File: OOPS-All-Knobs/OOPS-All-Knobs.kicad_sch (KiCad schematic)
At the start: 179 parts, among them J1 USB_C_Receptacle_USB2.0, J2 Conn_01x03_Female, SW1 SW_SPST, SW2 SW_SPST, U1 NCP1117-3.3_SOT223, U2 W25Q128JVS, U3 RP2040TR7, U4 SRV05-4, Y1 12MHz

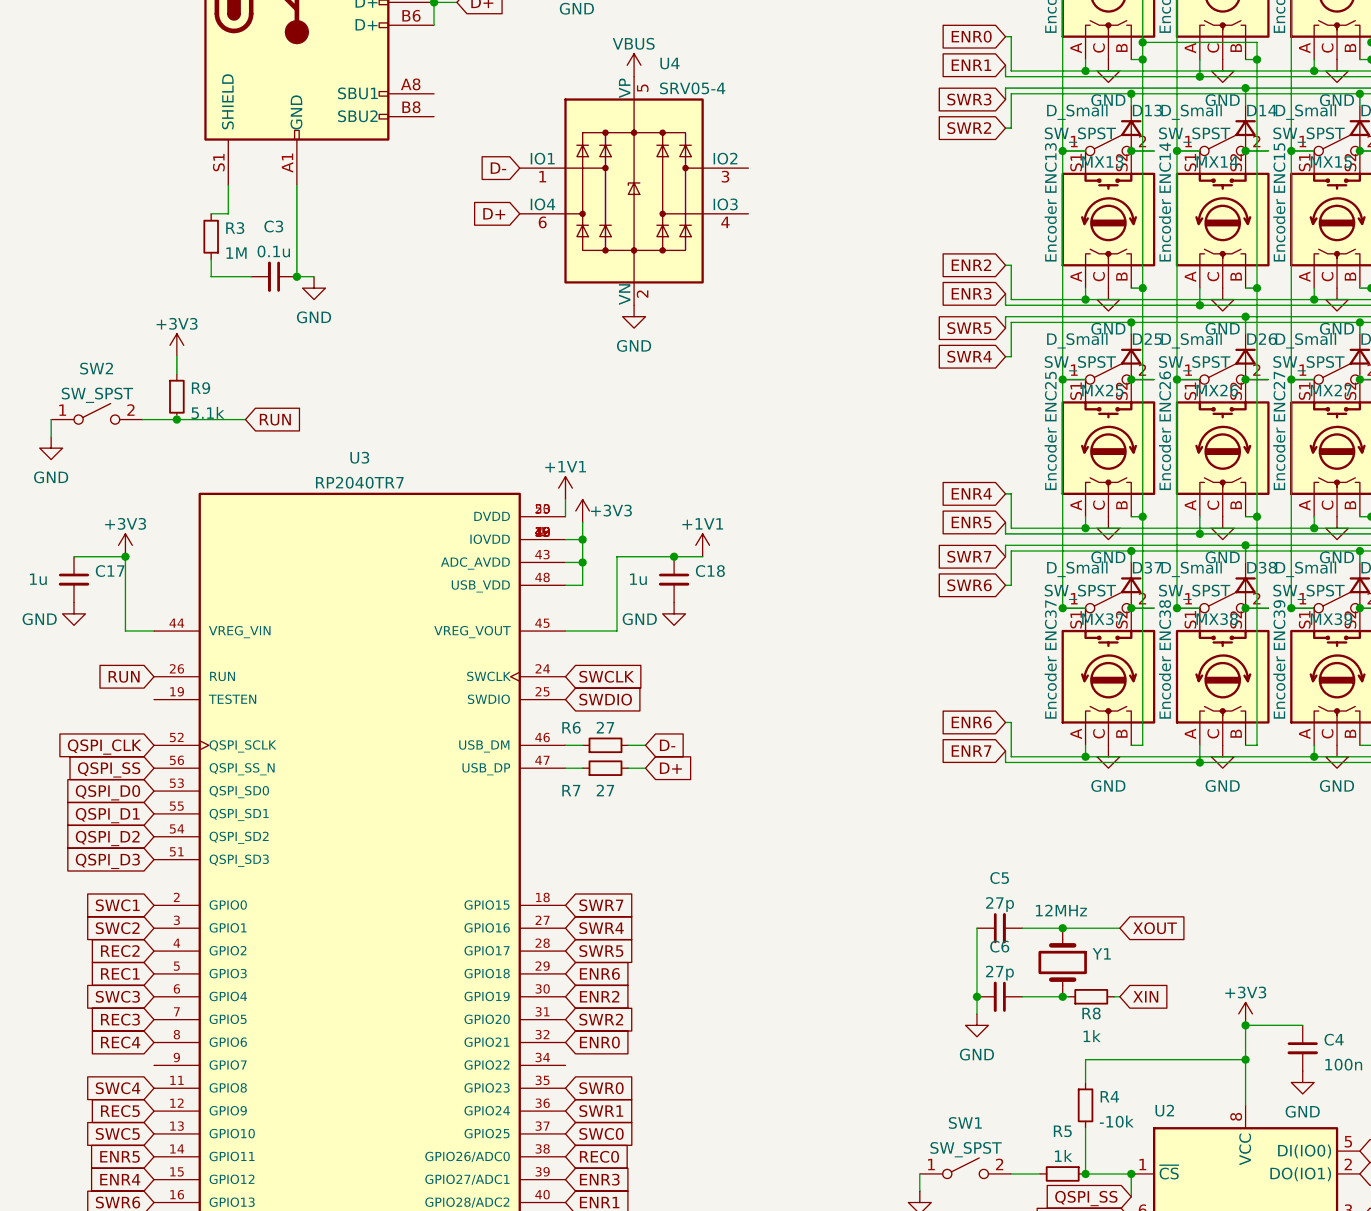
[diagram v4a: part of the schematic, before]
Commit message: Implemented proposed fixes for testgen, shielding, and xtal
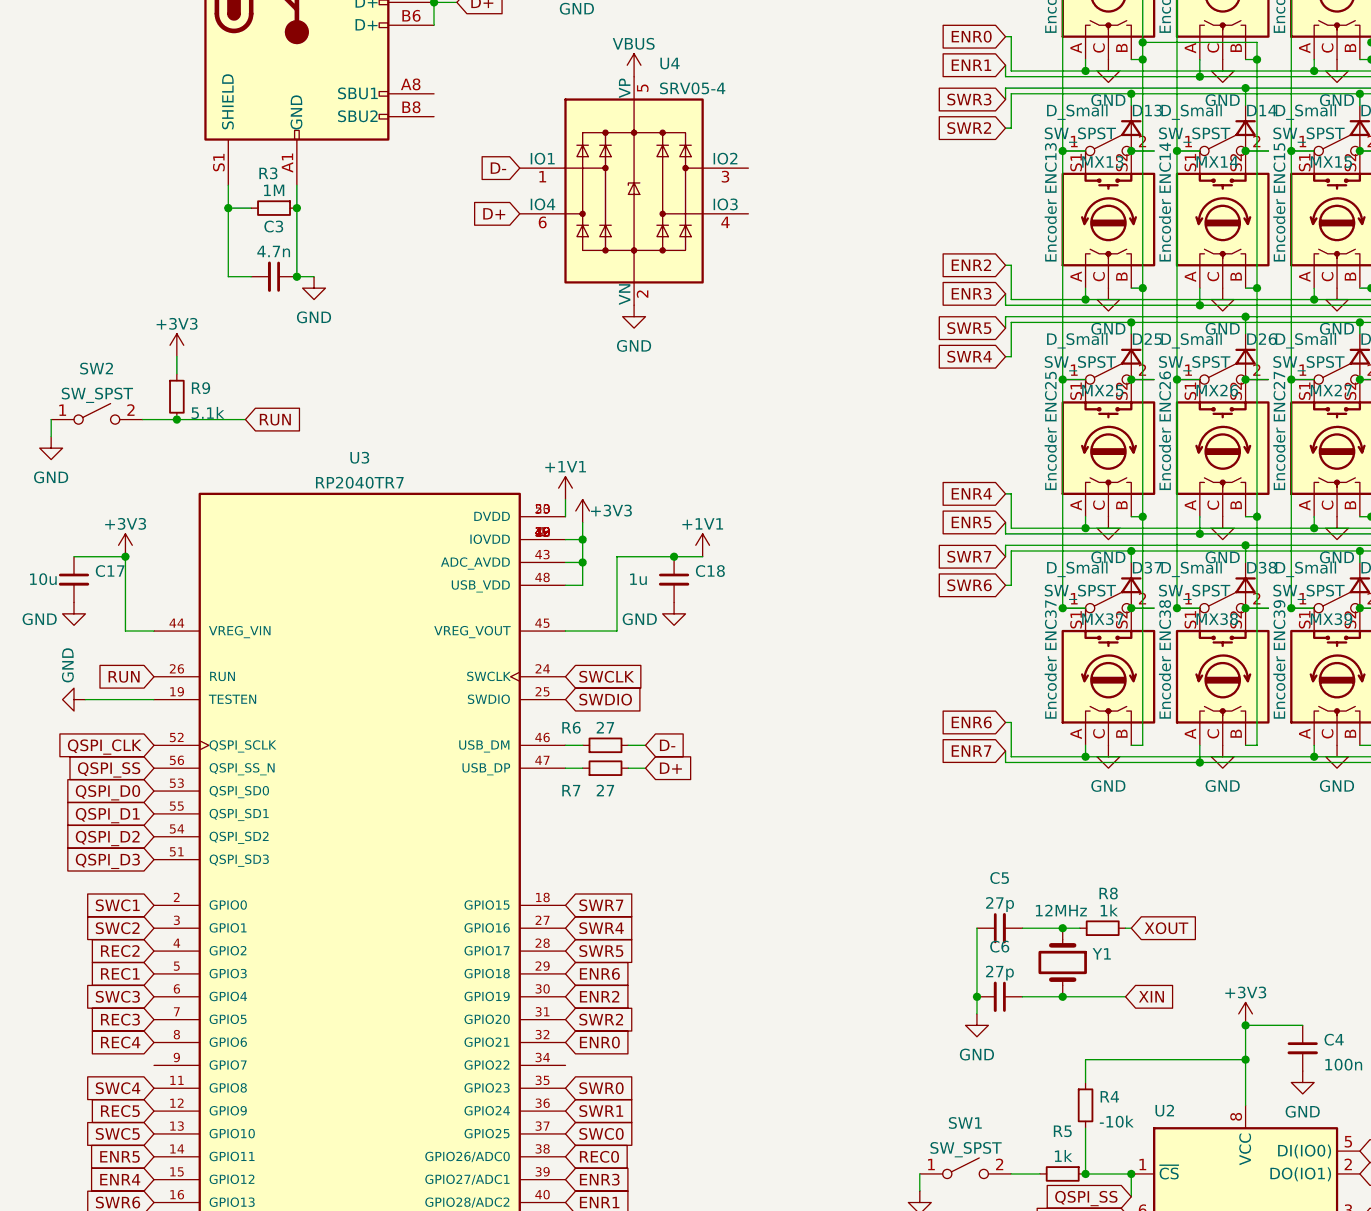
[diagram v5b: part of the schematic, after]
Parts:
- C17: value 1u -> 10u
- C3: value 0.1u -> 4.7n
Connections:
- net GND: now also R3.1, U3.19 (TESTEN)
- net XIN: now also C6.1, Y1.2; no longer R8.2
- net XOUT: now also R8.2; no longer C5.2, Y1.1
- net at C3.2: now also J1.S1 (SHIELD), R3.2; no longer R3.1
- new net: C5.2, R8.1, Y1.1
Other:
- moved on the sheet: R3, R8
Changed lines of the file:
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@@
   (junction (at 175.26 111.76) (diameter 0) (color 0 0 0 0)
   )
+  (junction (at 44.45 67.31) (diameter 0) (color 0 0 0 0)
+  )
   (junction (at 86.36 106.045) (diameter 0) (color 0 0 0 0)
   )
@@
   (junction (at 137.16 105.41) (diameter 0) (color 0 0 0 0)
   )
+  (junction (at 129.54 147.32) (diameter 0) (color 0 0 0 0)
+  )
   (junction (at 213.36 54.61) (diameter 0) (color 0 0 0 0)
   )
@@
   (junction (at 138.43 76.2) (diameter 0) (color 0 0 0 0)
   )
+  (junction (at 36.83 67.31) (diameter 0) (color 0 0 0 0)
+  )
   (junction (at 220.98 103.505) (diameter 0) (color 0 0 0 0)
   )
@@
   (junction (at 154.94 33.655) (diameter 0) (color 0 0 0 0)
   )
-  (junction (at 129.54 147.32) (diameter 0) (color 0 0 0 0)
-  )
   (junction (at 276.86 86.36) (diameter 0) (color 0 0 0 0)
   )
@@
     (stroke (width 0) (type default) (color 0 0 0 0))
   )
+  (wire (pts (xy 137.16 147.32) (xy 136.525 147.32))
+    (stroke (width 0) (type default) (color 0 0 0 0))
+  )
   (wire (pts (xy 201.93 50.8) (xy 201.93 76.2))
     (stroke (width 0) (type default) (color 0 0 0 0))
@@
     (stroke (width 0) (type default) (color 0 0 0 0))
   )
+  (wire (pts (xy 44.45 67.31) (xy 44.45 74.93))
+    (stroke (width 0) (type default) (color 0 0 0 0))
+  )
   (wire (pts (xy 137.16 80.01) (xy 162.56 80.01))
     (stroke (width 0) (type default) (color 0 0 0 0))
@@
     (stroke (width 0) (type default) (color 0 0 0 0))
   )
+  (wire (pts (xy 131.445 147.32) (xy 129.54 147.32))
+    (stroke (width 0) (type default) (color 0 0 0 0))
+  )
   (wire (pts (xy 175.26 53.975) (xy 175.26 55.88))
     (stroke (width 0) (type default) (color 0 0 0 0))
@@
     (stroke (width 0) (type default) (color 0 0 0 0))
   )
-  (wire (pts (xy 36.83 67.945) (xy 36.83 64.77))
+  (wire (pts (xy 36.83 64.77) (xy 36.83 67.31))
     (stroke (width 0) (type default) (color 0 0 0 0))
   )
@@
     (stroke (width 0) (type default) (color 0 0 0 0))
   )
+  (wire (pts (xy 20.955 121.92) (xy 28.575 121.92))
+    (stroke (width 0) (type default) (color 0 0 0 0))
+  )
   (wire (pts (xy 69.85 40.64) (xy 75.565 40.64))
     (stroke (width 0) (type default) (color 0 0 0 0))
@@
     (stroke (width 0) (type default) (color 0 0 0 0))
   )
-  (wire (pts (xy 135.255 154.94) (xy 135.89 154.94))
-    (stroke (width 0) (type default) (color 0 0 0 0))
-  )
   (wire (pts (xy 220.98 78.105) (xy 220.98 76.2))
     (stroke (width 0) (type default) (color 0 0 0 0))
@@
     (stroke (width 0) (type default) (color 0 0 0 0))
   )
-  (wire (pts (xy 34.925 73.025) (xy 34.925 74.93))
-    (stroke (width 0) (type default) (color 0 0 0 0))
-  )
   (wire (pts (xy 213.36 86.36) (xy 215.9 86.36))
     (stroke (width 0) (type default) (color 0 0 0 0))
@@
     (stroke (width 0) (type default) (color 0 0 0 0))
   )
+  (wire (pts (xy 36.83 67.31) (xy 39.37 67.31))
+    (stroke (width 0) (type default) (color 0 0 0 0))
+  )
   (wire (pts (xy 180.34 111.76) (xy 182.88 111.76))
     (stroke (width 0) (type default) (color 0 0 0 0))
@@
     (stroke (width 0) (type default) (color 0 0 0 0))
   )
+  (wire (pts (xy 36.83 74.93) (xy 39.37 74.93))
+    (stroke (width 0) (type default) (color 0 0 0 0))
+  )
   (wire (pts (xy 74.295 104.14) (xy 76.2 104.14))
     (stroke (width 0) (type default) (color 0 0 0 0))
@@
     (stroke (width 0) (type default) (color 0 0 0 0))
   )
-  (wire (pts (xy 34.925 67.945) (xy 36.83 67.945))
-    (stroke (width 0) (type default) (color 0 0 0 0))
-  )
   (wire (pts (xy 120.015 156.845) (xy 120.015 154.94))
     (stroke (width 0) (type default) (color 0 0 0 0))
@@
     (stroke (width 0) (type default) (color 0 0 0 0))
   )
-  (wire (pts (xy 129.54 154.94) (xy 130.175 154.94))
+  (wire (pts (xy 129.54 154.94) (xy 136.525 154.94))
     (stroke (width 0) (type default) (color 0 0 0 0))
   )
@@
     (stroke (width 0) (type default) (color 0 0 0 0))
   )
-  (wire (pts (xy 34.925 74.93) (xy 39.37 74.93))
-    (stroke (width 0) (type default) (color 0 0 0 0))
-  )
   (wire (pts (xy 120.015 147.32) (xy 120.015 154.94))
     (stroke (width 0) (type default) (color 0 0 0 0))
@@
     (stroke (width 0) (type default) (color 0 0 0 0))
   )
-  (wire (pts (xy 129.54 147.32) (xy 135.89 147.32))
-    (stroke (width 0) (type default) (color 0 0 0 0))
-  )
   (wire (pts (xy 240.03 50.8) (xy 240.03 48.895))
     (stroke (width 0) (type default) (color 0 0 0 0))
@@
     (stroke (width 0) (type default) (color 0 0 0 0))
   )
-  (wire (pts (xy 44.45 64.77) (xy 44.45 74.93))
+  (wire (pts (xy 44.45 64.77) (xy 44.45 67.31))
     (stroke (width 0) (type default) (color 0 0 0 0))
   )
@@
     (stroke (width 0) (type default) (color 0 0 0 0))
   )
+  (wire (pts (xy 36.83 67.31) (xy 36.83 74.93))
+    (stroke (width 0) (type default) (color 0 0 0 0))
+  )
   (wire (pts (xy 173.99 149.86) (xy 182.245 149.86))
     (stroke (width 0) (type default) (color 0 0 0 0))
@@
     )
   )
-  (global_label "XIN" (shape input) (at 135.89 154.94 0) (fields_autoplaced)
+  (global_label "XIN" (shape input) (at 136.525 154.94 0) (fields_autoplaced)
     (effects (font (size 1.27 1.27)) (justify left))
-    (property "Intersheet References" "${INTERSHEET_REFS}" (id 0) (at 141.4479 154.8606 0)
+    (property "Intersheet References" "${INTERSHEET_REFS}" (id 0) (at 142.0829 154.8606 0)
       (effects (font (size 1.27 1.27)) (justify left) hide)
     )
@@
     )
   )
-  (global_label "XOUT" (shape input) (at 135.89 147.32 0) (fields_autoplaced)
+  (global_label "XOUT" (shape input) (at 137.16 147.32 0) (fields_autoplaced)
     (effects (font (size 1.27 1.27)) (justify left))
-    (property "Intersheet References" "${INTERSHEET_REFS}" (id 0) (at 143.1412 147.2406 0)
+    (property "Intersheet References" "${INTERSHEET_REFS}" (id 0) (at 144.4112 147.2406 0)
       (effects (font (size 1.27 1.27)) (justify left) hide)
     )
@@
     (pin "S2")
   )
-  (symbol (lib_id "Device:R_Small") (at 132.715 154.94 90) (unit 1)
+  (symbol (lib_id "Device:R_Small") (at 133.985 147.32 90) (unit 1)
     (in_bom yes) (on_board yes)
-    (property "Reference" "R8" (id 0) (at 132.715 156.845 90))
-    (property "Value" "1k" (id 1) (at 132.715 159.385 90))
-    (property "Footprint" "Resistor_SMD:R_0402_1005Metric" (id 2) (at 132.715 154.94 0)
+    (property "Reference" "R8" (id 0) (at 134.62 143.51 90))
+    (property "Value" "1k" (id 1) (at 134.62 145.415 90))
+    (property "Footprint" "Resistor_SMD:R_0402_1005Metric" (id 2) (at 133.985 147.32 0)
       (effects (font (size 1.27 1.27)) hide)
     )
-    (property "Datasheet" "~" (id 3) (at 132.715 154.94 0)
+    (property "Datasheet" "~" (id 3) (at 133.985 147.32 0)
       (effects (font (size 1.27 1.27)) hide)
     )
@@
     (in_bom yes) (on_board yes) (fields_autoplaced)
     (property "Reference" "C3" (id 0) (at 41.9036 69.4014 90))
-    (property "Value" "0.1u" (id 1) (at 41.9036 72.1765 90))
+    (property "Value" "4.7n" (id 1) (at 41.9036 72.1765 90))
     (property "Footprint" "Capacitor_SMD:C_0402_1005Metric" (id 2) (at 41.91 74.93 0)
       (effects (font (size 1.27 1.27)) hide)
@@
     (pin "2")
   )
+  (symbol (lib_id "power:GND") (at 20.955 121.92 270) (unit 1)
+    (in_bom yes) (on_board yes)
+    (property "Reference" "#PWR0116" (id 0) (at 14.605 121.92 0)
+      (effects (font (size 1.27 1.27)) hide)
+    )
+    (property "Value" "GND" (id 1) (at 19.05 118.11 0))
+    (property "Footprint" "" (id 2) (at 20.955 121.92 0)
+      (effects (font (size 1.27 1.27)) hide)
+    )
+    (property "Datasheet" "" (id 3) (at 20.955 121.92 0)
+      (effects (font (size 1.27 1.27)) hide)
+    )
+    (pin "1")
+  )
   (symbol (lib_id "power:GND") (at 274.32 50.8 0) (unit 1)
     (in_bom yes) (on_board yes) (fields_autoplaced)
@@
     (pin "2")
   )
-  (symbol (lib_id "Device:R_Small") (at 34.925 70.485 180) (unit 1)
-    (in_bom yes) (on_board yes) (fields_autoplaced)
-    (property "Reference" "R3" (id 0) (at 36.4236 69.5765 0)
-      (effects (font (size 1.27 1.27)) (justify right))
-    )
-    (property "Value" "1M" (id 1) (at 36.4236 72.3516 0)
-      (effects (font (size 1.27 1.27)) (justify right))
-    )
-    (property "Footprint" "Resistor_SMD:R_0402_1005Metric" (id 2) (at 34.925 70.485 0)
+  (symbol (lib_id "Device:R_Small") (at 41.91 67.31 270) (unit 1)
+    (in_bom yes) (on_board yes)
+    (property "Reference" "R3" (id 0) (at 41.275 63.5 90))
+    (property "Value" "1M" (id 1) (at 41.91 65.382 90))
+    (property "Footprint" "Resistor_SMD:R_0402_1005Metric" (id 2) (at 41.91 67.31 0)
       (effects (font (size 1.27 1.27)) hide)
     )
-    (property "Datasheet" "~" (id 3) (at 34.925 70.485 0)
+    (property "Datasheet" "~" (id 3) (at 41.91 67.31 0)
       (effects (font (size 1.27 1.27)) hide)
     )
@@
       (effects (font (size 1.27 1.27)) (justify left))
     )
-    (property "Value" "1u" (id 1) (at 14.605 108.585 0)
+    (property "Value" "10u" (id 1) (at 14.605 108.585 0)
       (effects (font (size 1.27 1.27)) (justify left))
     )
@@
       (reference "#PWR0115") (unit 1) (value "GND") (footprint "")
     )
+    (path "/cffd5d0a-6d1c-4788-bf09-03d483af01df"
+      (reference "#PWR0116") (unit 1) (value "GND") (footprint "")
+    )
     (path "/bdd77c0d-a2aa-4b58-9914-4ae81a1f5790"
       (reference "C1") (unit 1) (value "10u") (footprint "Capacitor_SMD:C_0402_1005Metric")
@@
     )
     (path "/63b939d7-fc3d-4bd1-9e30-690bb9772c7b"
-      (reference "C3") (unit 1) (value "0.1u") (footprint "Capacitor_SMD:C_0402_1005Metric")
+      (reference "C3") (unit 1) (value "4.7n") (footprint "Capacitor_SMD:C_0402_1005Metric")
     )
     (path "/d7aa911c-b472-4631-9e24-2bb8180dffd9"
@@
     )
     (path "/e734ad59-b452-4b44-9d11-eb0d2d2e6515"
-      (reference "C17") (unit 1) (value "1u") (footprint "Capacitor_SMD:C_0402_1005Metric")
+      (reference "C17") (unit 1) (value "10u") (footprint "Capacitor_SMD:C_0402_1005Metric")
     )
     (path "/8d421297-29d2-4b87-9e40-0c41d2b60e5a"

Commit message: a few more improvements
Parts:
- added C15: 10u, Capacitor_SMD:C_0402_1005Metric, symbol Device:C_Small
- C17: value 10u -> 1u
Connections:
- net +3V3: now also C15.1
- net GND: now also C15.2
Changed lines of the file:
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@@
   (junction (at 182.88 52.07) (diameter 0) (color 0 0 0 0)
   )
+  (junction (at 26.67 106.045) (diameter 0) (color 0 0 0 0)
+  )
   (junction (at 200.66 60.96) (diameter 0) (color 0 0 0 0)
   )
@@
   (junction (at 208.28 52.07) (diameter 0) (color 0 0 0 0)
   )
+  (junction (at 19.685 111.125) (diameter 0) (color 0 0 0 0)
+  )
   (junction (at 200.66 86.36) (diameter 0) (color 0 0 0 0)
   )
@@
   (junction (at 142.24 60.96) (diameter 0) (color 0 0 0 0)
   )
+  (junction (at 25.4 106.045) (diameter 0) (color 0 0 0 0)
+  )
   (junction (at 226.06 53.975) (diameter 0) (color 0 0 0 0)
   )
@@
   (junction (at 167.64 111.76) (diameter 0) (color 0 0 0 0)
   )
-  (junction (at 25.4 106.045) (diameter 0) (color 0 0 0 0)
-  )
   (junction (at 59.69 44.45) (diameter 0) (color 0 0 0 0)
   )
@@
     (stroke (width 0) (type default) (color 0 0 0 0))
   )
+  (wire (pts (xy 19.685 111.125) (xy 26.67 111.125))
+    (stroke (width 0) (type default) (color 0 0 0 0))
+  )
   (wire (pts (xy 226.06 76.2) (xy 227.33 76.2))
     (stroke (width 0) (type default) (color 0 0 0 0))
@@
     (stroke (width 0) (type default) (color 0 0 0 0))
   )
-  (wire (pts (xy 25.4 106.045) (xy 25.4 114.3))
-    (stroke (width 0) (type default) (color 0 0 0 0))
-  )
   (wire (pts (xy 144.78 128.905) (xy 170.18 128.905))
     (stroke (width 0) (type default) (color 0 0 0 0))
@@
     (stroke (width 0) (type default) (color 0 0 0 0))
   )
+  (wire (pts (xy 26.67 106.045) (xy 28.575 106.045))
+    (stroke (width 0) (type default) (color 0 0 0 0))
+  )
   (wire (pts (xy 269.24 60.96) (xy 269.24 86.36))
     (stroke (width 0) (type default) (color 0 0 0 0))
@@
     (stroke (width 0) (type default) (color 0 0 0 0))
   )
+  (wire (pts (xy 25.4 106.045) (xy 26.67 106.045))
+    (stroke (width 0) (type default) (color 0 0 0 0))
+  )
   (wire (pts (xy 100.965 26.67) (xy 108.585 26.67))
     (stroke (width 0) (type default) (color 0 0 0 0))
@@
     (stroke (width 0) (type default) (color 0 0 0 0))
   )
+  (wire (pts (xy 28.575 114.3) (xy 28.575 106.045))
+    (stroke (width 0) (type default) (color 0 0 0 0))
+  )
   (wire (pts (xy 80.01 114.3) (xy 80.01 106.045))
     (stroke (width 0) (type default) (color 0 0 0 0))
@@
     (stroke (width 0) (type default) (color 0 0 0 0))
   )
-  (wire (pts (xy 25.4 114.3) (xy 28.575 114.3))
-    (stroke (width 0) (type default) (color 0 0 0 0))
-  )
   (wire (pts (xy 246.38 103.505) (xy 271.78 103.505))
     (stroke (width 0) (type default) (color 0 0 0 0))
@@
     (pin "S2")
   )
+  (symbol (lib_id "Device:C_Small") (at 26.67 108.585 0) (unit 1)
+    (in_bom yes) (on_board yes)
+    (property "Reference" "C15" (id 0) (at 21.59 110.49 0)
+      (effects (font (size 1.27 1.27)) (justify left))
+    )
+    (property "Value" "10u" (id 1) (at 21.59 108.585 0)
+      (effects (font (size 1.27 1.27)) (justify left))
+    )
+    (property "Footprint" "Capacitor_SMD:C_0402_1005Metric" (id 2) (at 26.67 108.585 0)
+      (effects (font (size 1.27 1.27)) hide)
+    )
+    (property "Datasheet" "~" (id 3) (at 26.67 108.585 0)
+      (effects (font (size 1.27 1.27)) hide)
+    )
+    (pin "1")
+    (pin "2")
+  )
   (symbol (lib_id "Device:Rotary_Encoder_Switch") (at 261.62 43.18 90) (unit 1)
     (in_bom yes) (on_board yes)
@@
   (symbol (lib_id "Device:C_Small") (at 19.685 108.585 0) (unit 1)
     (in_bom yes) (on_board yes)
-    (property "Reference" "C17" (id 0) (at 22.0091 107.6828 0)
+    (property "Reference" "C17" (id 0) (at 13.97 110.49 0)
       (effects (font (size 1.27 1.27)) (justify left))
     )
-    (property "Value" "10u" (id 1) (at 14.605 108.585 0)
+    (property "Value" "1u" (id 1) (at 14.605 108.585 0)
       (effects (font (size 1.27 1.27)) (justify left))
     )
@@
       (reference "C14") (unit 1) (value "100n") (footprint "Capacitor_SMD:C_0402_1005Metric")
     )
+    (path "/0ae07051-7ebf-4e91-819f-f40ac7eb87c4"
+      (reference "C15") (unit 1) (value "10u") (footprint "Capacitor_SMD:C_0402_1005Metric")
+    )
     (path "/e734ad59-b452-4b44-9d11-eb0d2d2e6515"
-      (reference "C17") (unit 1) (value "10u") (footprint "Capacitor_SMD:C_0402_1005Metric")
+      (reference "C17") (unit 1) (value "1u") (footprint "Capacitor_SMD:C_0402_1005Metric")
     )
     (path "/8d421297-29d2-4b87-9e40-0c41d2b60e5a"
